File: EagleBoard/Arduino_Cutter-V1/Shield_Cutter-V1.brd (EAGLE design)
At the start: 68.9 x 53.7 mm, 82 parts, among them IC1 L298P, IC2 REG1117, K1 AQY21SOP, K2 AQY21SOP, U1 ARDUINOR3-DIMENSION, X1 2514-, X2 22-23-2041, X3 22-23-2021, X4 22-23-2021

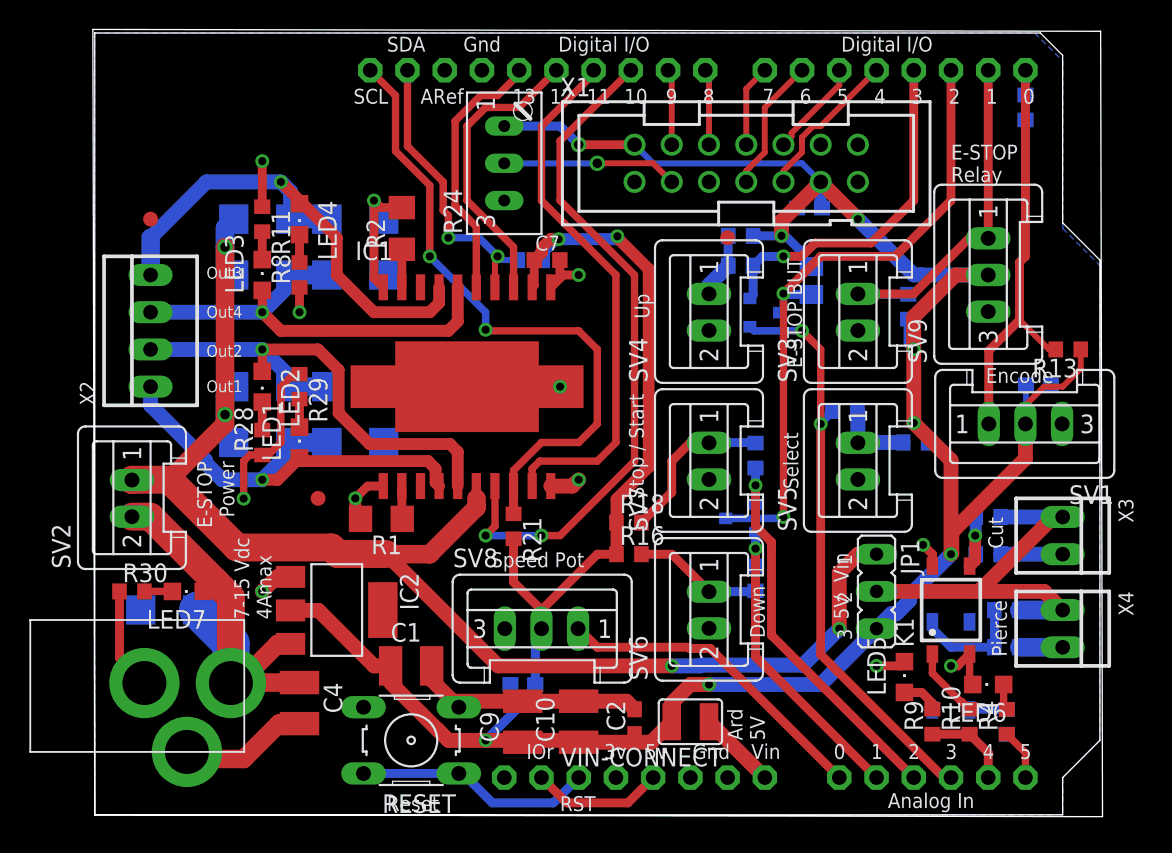
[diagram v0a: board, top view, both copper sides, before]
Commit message: FIX: increase components to 0805 size
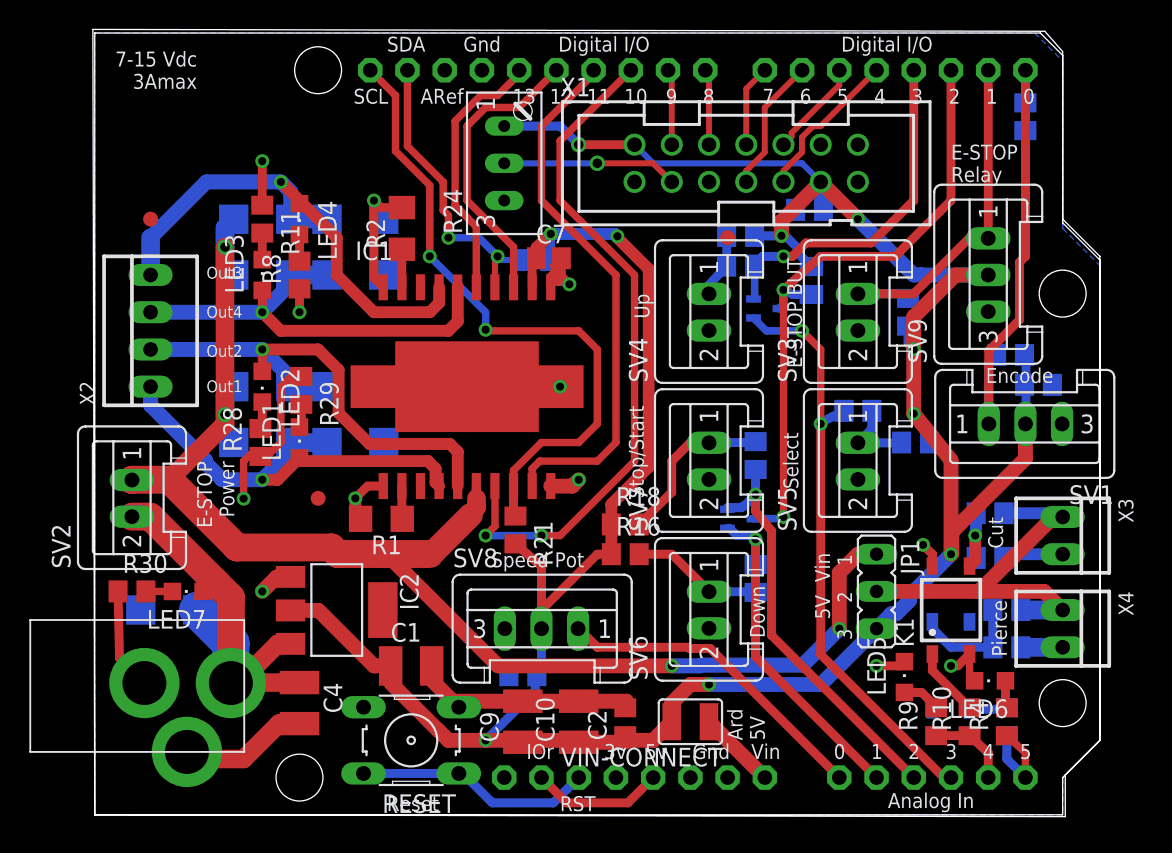
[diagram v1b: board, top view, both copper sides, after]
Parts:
- C11, C2, C5, C6: device rcl:C0603 -> rcl:C0805
- C7: device SmartPrj:C0603K -> SmartPrj:C0805
- D11, D12: device zetex:SOT-23 -> zetex:SOT323
- R10, R11, R12, R13, R14, R15, R16, R17, R18, R20, R21, R22, R23, R25, R26, R27, R28, R29, R3, R30, R4, R5, R6, R7, R8, R9: device resistor:R0603 -> resistor:R0805
- RESET: value (none) -> 1
- SV1, SV8, SV9: value (none) -> S3B-PH-K
- SV2, SV3, SV4, SV5, SV6, SV7: value (none) -> S2B-PH-K
- moved R13 3.96 mm to (62.5, 31.4), flipped to the bottom, turned to 0 degrees
- moved R25 0.89 mm to (52.1, 27.6)
- moved C11 0.63 mm to (29.2, 9.53)
- moved C2 0.63 mm to (36.2, 6.35)
- moved R14 0.63 mm to (63.5, 47.6)
- moved R20 0.38 mm to (55.5, 34.3)
- moved R22 0.38 mm to (30.1, 37.8)
- moved R12 0.28 mm to (61.1, 20.6)
- moved R3 0.28 mm to (61.1, 17.5)
- moved LED6 0.28 mm to (61.1, 9.14)
- moved R29 0.28 mm to (14.1, 29.0)
- moved D11 0.28 mm to (45.8, 34.5), turned to 90 degrees
- moved R21 0.28 mm to (28.7, 19.4)
- moved R18 0.28 mm to (36.2, 19.8)
- moved R9 0.25 mm to (57.4, 6.35)
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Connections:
- net SELECT_BUT: now also D11.2; no longer D11.3
- net UP_BUT: now also D11.3; no longer D11.2
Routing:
- net GND: track 95.8 -> 91.1 mm
- net SOL_PIERCE: track 3.49 -> 6.80 mm
- net DOWN_BUT: track 21.3 -> 23.6 mm
- net ENCODER1: track 30.2 -> 32.3 mm
- net BUTTON_INT: track 45.5 -> 43.7 mm
- net +5V: track 213.4 -> 212.1 mm
- net ENABLEA: track 44.2 -> 45.4 mm
- net RUN_BUT: track 26.9 -> 27.8 mm
- net SELECT_BUT: track 39.9 -> 40.5 mm
- net N$16: track 4.78 -> 5.29 mm
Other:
- board size 68.9 x 53.7 mm -> 68.7 x 53.7 mm
- board text added: "7-15 Vdc 3Amax"
- board text added: "CUT1-V1.0 8-17"
- board text added: "Stop/Start"
- board text removed: "7-15 Vdc 4Amax"
- board text removed: "CUT1-V1.0"
- board text removed: "Stop / Start"

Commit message: Chore: gerbers and files for pcb manufacture
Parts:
- removed LED7: Green, led:CHIPLED_0805
- removed R30: 1kΩ, resistor:R0805
- added X5: 22-23-2021, con-molex:22-23-2021
- moved FID3 6.98 mm to (3.81, 47.6)
- moved SV2 4.49 mm to (3.17, 26.0)
- moved X2 4.49 mm to (3.17, 37.5)
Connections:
- removed net N$18: LED7.C, R30.2
- removed net OUT5: C4.1, D10.P$1, IC2.3, LED7.A, SV2.2, U$2.TIP
- new net FUSE_RETURN: C4.1, D10.P$1, IC2.3, SV2.2, X5.2
- new net POWERIN: U$2.TIP, X5.1
- net GND: no longer R30.1
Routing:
- net OUT5: track 31.2 -> 0.00 mm
- net FUSE_RETURN: track 0.00 -> 30.3 mm
- net POWERIN: track 0.00 -> 10.8 mm
- net VMOT: track 96.5 -> 102.6 mm
- net GND: track 91.1 -> 86.2 mm
- net OUT1: track 31.1 -> 35.8 mm
- net OUT3: track 37.6 -> 34.9 mm
- net OUT4: track 31.7 -> 34.2 mm
- net OUT2: track 34.9 -> 37.3 mm
- net N$18: track 1.81 -> 0.00 mm
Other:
- board text added: "Encoder"
- board text added: "Fuse"
- board text added: "Sol 1"
- board text added: "Sol 2"
- board text removed: "Cut"
- board text removed: "Encode"
- board text removed: "Pierce"

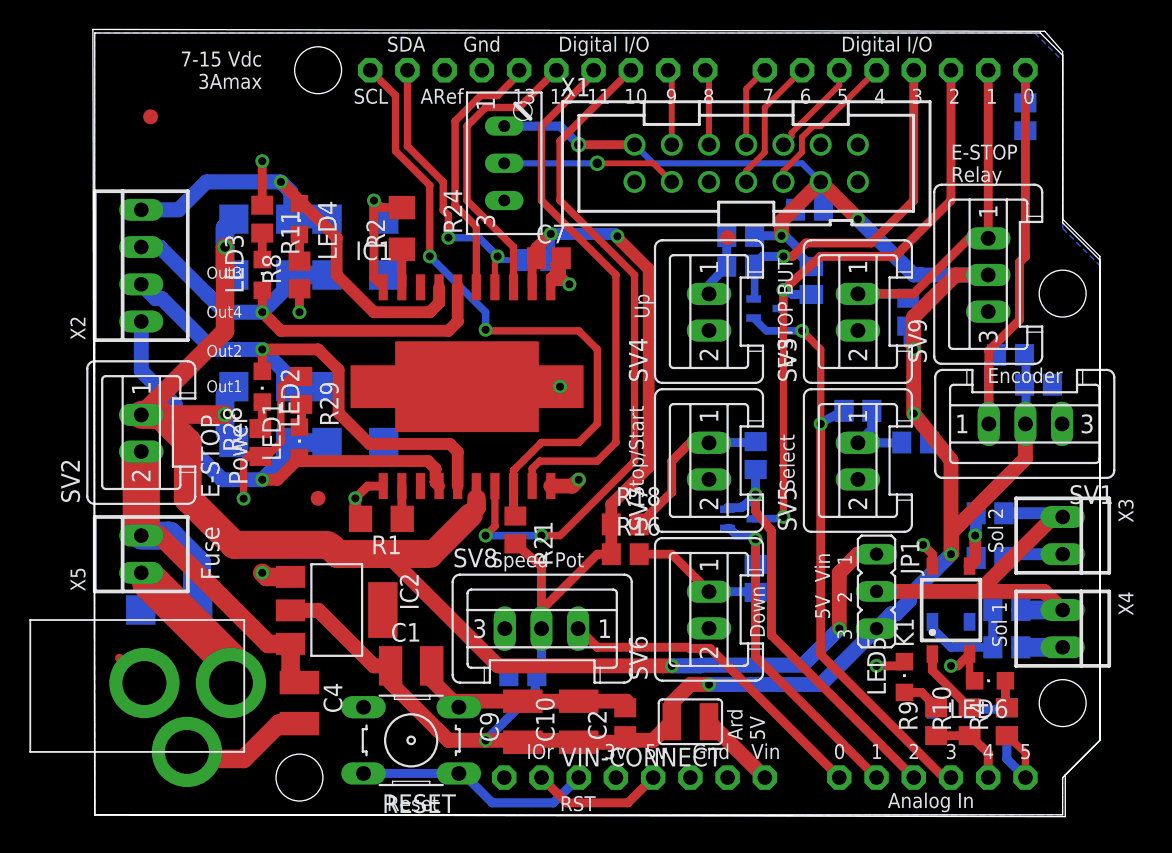
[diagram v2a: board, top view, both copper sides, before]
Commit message: Chore: add part names to pcb and cap from vmot to ground
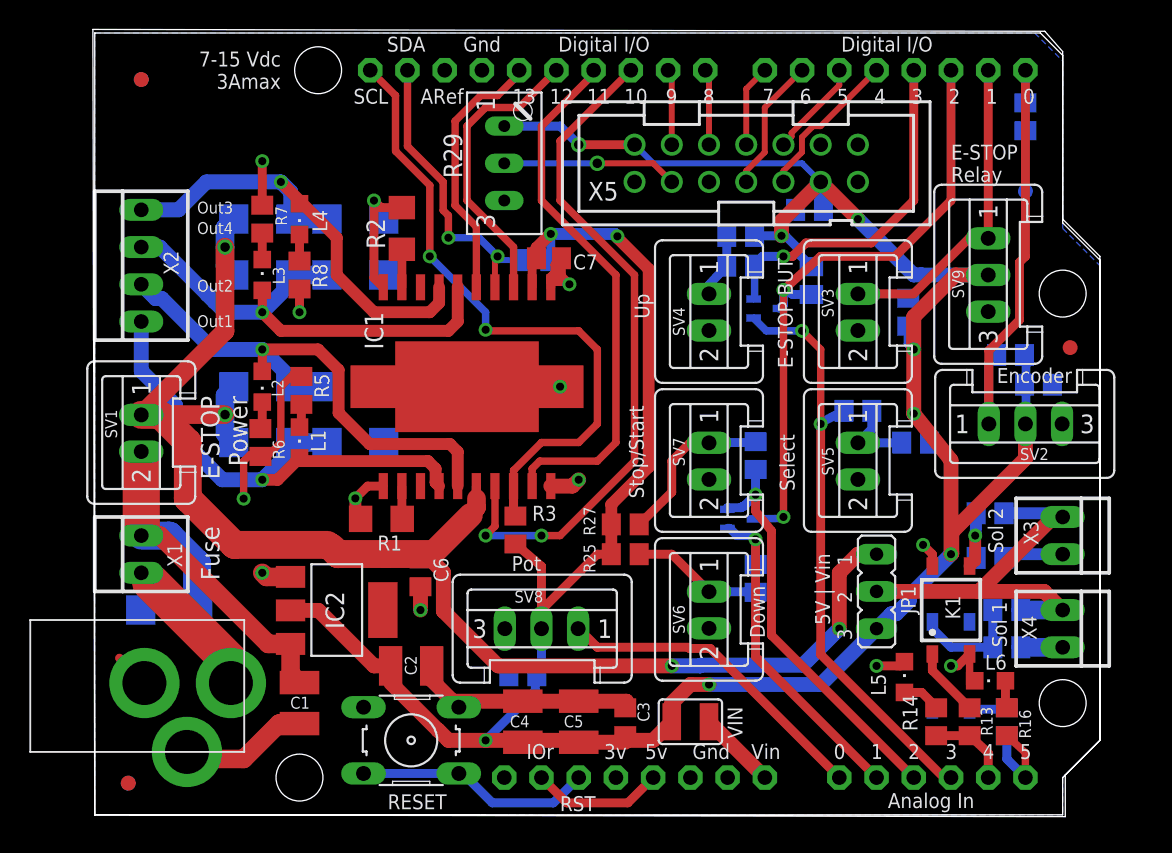
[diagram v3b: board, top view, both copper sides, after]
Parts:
- removed C11: 100nF, rcl:C0805
- removed D12: 40v, zetex:SOT323
- added C3, C8: 100nF, rcl:C0805
- added D9: SS14, SmartPrj:SMA
- added FID4, FID5, FID6: FIDUCIALMOUNT, SmartPrj:FIDUCIA-MOUNT
- C10, C9: value 10u 35V -> 100nF; device SmartPrj:C1210 -> rcl:C0805
- C2, C5: value 100nF -> 10u 35V; device rcl:C0805 -> SmartPrj:C1210
- C7: value 100n -> 100nF
- D10: value SS14 -> 40v; device SmartPrj:SMA -> zetex:SOT323
- R10: value 2.5kΩ -> 10kΩ
- R11, R28: value 1kΩ -> 10Ω
- R13, R14, R15, R16: value 10kΩ -> 330Ω
- R19: device resistor:M0805 -> resistor:R0805
- R21: value 10kΩ -> 10Ω
- R22: device resistor:R0805 -> resistor:M0805
- R23, R25, R27, R3: value 10Ω -> 10kΩ
- R24: value 10k -> 10Ω; device pot:S64W -> resistor:R0805
- R29: value 1kΩ -> 10k; device resistor:R0805 -> pot:S64W
- R4: value 300Ω -> 10kΩ
- R5: value 10kΩ -> 1kΩ
- R6: value 2.5kΩ -> 1kΩ
- R7: value 10Ω -> 1kΩ
- R9: value 300Ω -> 10Ω
- SV1: value S3B-PH-K -> S2B-PH-K; device con-amp-mt:S03P -> con-amp-mt:S02P
- SV2: value S2B-PH-K -> S3B-PH-K; device con-amp-mt:S02P -> con-amp-mt:S03P
- X1: value 2514- -> 22-23-2021; device con-3m:PAK100/2500-14 -> con-molex:22-23-2021
- X5: value 22-23-2021 -> 2514-; device con-molex:22-23-2021 -> con-3m:PAK100/2500-14
- moved SV1 60.3 mm to (3.17, 26.0), turned to 90 degrees
- moved SV2 60.3 mm to (63.5, 26.7), turned to 180 degrees
- moved R11 58.6 mm to (62.2, 11.4), flipped to the bottom, turned to 180 degrees
- moved R7 58.6 mm to (11.4, 40.6), flipped to the top, turned to 270 degrees
- moved R6 54.4 mm to (11.3, 25.4), flipped to the top
- moved R5 50.4 mm to (14.1, 29.0), flipped to the top, turned to 270 degrees
- moved X1 49.1 mm to (3.17, 17.8), turned to 90 degrees
- moved X5 49.1 mm to (44.5, 44.5), turned to 0 degrees
- moved D10 45.7 mm to (45.8, 34.5), turned to 90 degrees
- moved R4 45.0 mm to (30.1, 37.8), flipped to the bottom, turned to 0 degrees
- moved R14 41.7 mm to (57.4, 6.35), flipped to the top
- moved C5 38.9 mm to (33.0, 6.35), flipped to the top, turned to 90 degrees
- moved C10 38.3 mm to (48.8, 41.3), flipped to the bottom, turned to 180 degrees
- moved R15 37.8 mm to (62.2, 6.35), turned to 90 degrees
- moved C6 36.3 mm to (22.2, 16.5), flipped to the top, turned to 90 degrees
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- renumbered LED1 to L1, LED2 to L2, LED3 to L3, LED4 to L4, LED5 to L5, LED6 to L6, VIN-CONNECT to VIN
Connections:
- net +5V: now also C10.2, C3.1, C4.1, C8.1, R23.1, R25.1, R27.1, R29.A, R3.2, R4.1, SV2.2, X5.11, X5.2; no longer C1.1, C10.1, C11.1, C6.2, R13.1, R15.1, R16.1, R17.1, R21.2, R24.A, SV1.2, X1.11, X1.2
- net BUTTON_INT: now also D10.1, R22.2; no longer D12.1, R19.2
- net DOWN_BUT: now also D11.2; no longer D12.2
- net E-STOP: now also R19.2; no longer R20.2
- net ENABLEA: now also R3.1; no longer R21.1
- net ENABLEB: now also R4.2; no longer R22.2
- net ENCODER1: now also R17.2, R18.2, SV2.1; no longer R13.2, R14.2, SV1.1
- net FUSE_RETURN: now also C1.1, D9.P$1, SV1.2, X1.2; no longer C4.1, D10.P$1, SV2.2, X5.2
- net GND: now also C10.1, C3.2, C8.2, D9.P$2, R17.1, R29.E, R5.1, R6.1, R7.1, SV2.3, X5.1, X5.12, X5.5; no longer C10.2, C11.2, D10.P$2, R11.1, R14.1, R24.E, R28.1, R29.1, SV1.3, X1.1, X1.12, X1.5
- net LCD_D4: now also X5.8; no longer X1.8
- net LCD_D5: now also X5.7; no longer X1.7
- net LCD_D6: now also X5.10; no longer X1.10
- net LCD_D7: now also X5.9; no longer X1.9
- net LCD_EN: now also X5.6; no longer X1.6
- net LCD_RS: now also X5.4; no longer X1.4
- net N$10: now also R10.2; no longer R5.2
- net N$11: now also R11.1, R12.1; no longer R5.1, R7.1
- net N$12: now also R16.2; no longer R4.2
- net N$13: now also R20.2, R21.1; no longer R15.2, R23.1
- net N$14: now also R15.2; no longer R6.2
- net N$15: now also R11.2; no longer R7.2
- net N$16: now also R10.1, R9.1; no longer R12.1, R3.1
- net N$17: now also R25.2; no longer R16.2
- net N$19: now also R27.2, R28.1; no longer R18.2, R27.1
- net N$2: now also R7.2; no longer R11.2
- net N$3: now also R6.2; no longer R28.2
- net N$4: now also R5.2; no longer R29.2
- net N$5: now also R13.2; no longer R10.2
- net N$7: now also R14.2; no longer R9.2
- net N$8: now also R9.2; no longer R3.2
- net N$9: now also R23.2, R24.1; no longer R17.2, R25.1
- net POWERIN: now also X1.1; no longer X5.1
- net RUN_BUT: now also D11.3, R28.2; no longer D12.3, R27.2
- net SELECT_BUT: now also D10.2, R24.2; no longer D11.2, R25.2
- net SOL_CUT: now also R13.1, R14.1; no longer R10.1, R9.1
- net SOL_PIERCE: now also R15.1, R16.1; no longer R4.1, R6.1
- net UP_BUT: now also D10.3, R21.2; no longer D11.3, R23.2
- net V0: now also R29.S, X5.3; no longer R24.S, X1.3
- net VMOT: now also C6.2, SV1.1; no longer SV2.1
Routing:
- net GND: track 86.2 -> 87.8 mm, vias 11 -> 12
- net VMOT: track 102.6 -> 102.1 mm
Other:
- board text added: "5V | Vin"
- board text added: "Pot"
- board text removed: "5V"
- board text removed: "Ard 5V"
- board text removed: "Reset"
- board text removed: "Speed Pot"
- board text removed: "Vin"

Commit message: Fix: fix floating ground. Feat: add power input terminal.
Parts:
- removed SV1: S2B-PH-K, con-amp-mt:S02P
- added X6: 22-23-2021, con-molex:22-23-2021
- X1: value 22-23-2021 -> 22-23-2041; device con-molex:22-23-2021 -> con-molex:22-23-2041
- moved X1 1.90 mm to (3.17, 19.7)
- moved D9 0.63 mm to (5.08, 13.3)
- turned JP1 to 90 degrees
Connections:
- net FUSE_RETURN: now also X1.4, X6.1; no longer SV1.2, X1.2
- net GND: now also X1.1
- net POWERIN: now also X1.2, X1.3; no longer X1.1
- net VMOT: now also X6.2; no longer SV1.1
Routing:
- net VMOT: track 102.1 -> 94.5 mm, vias 4 -> 3
- net POWERIN: track 10.8 -> 15.9 mm
- net FUSE_RETURN: track 30.3 -> 26.5 mm, vias 0 -> 1
- net GND: track 87.8 -> 84.3 mm, vias 12 -> 28
- net +5V: track 212.1 -> 212.9 mm
- net OUT1: track 35.8 -> 36.4 mm
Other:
- board text added: "CUT1-V1.1 8-17"
- board text added: "GND"
- board text added: "V+"
- board text added: "Vin | 5V"
- board text removed: "5V | Vin"
- board text removed: "CUT1-V1.0 8-17"

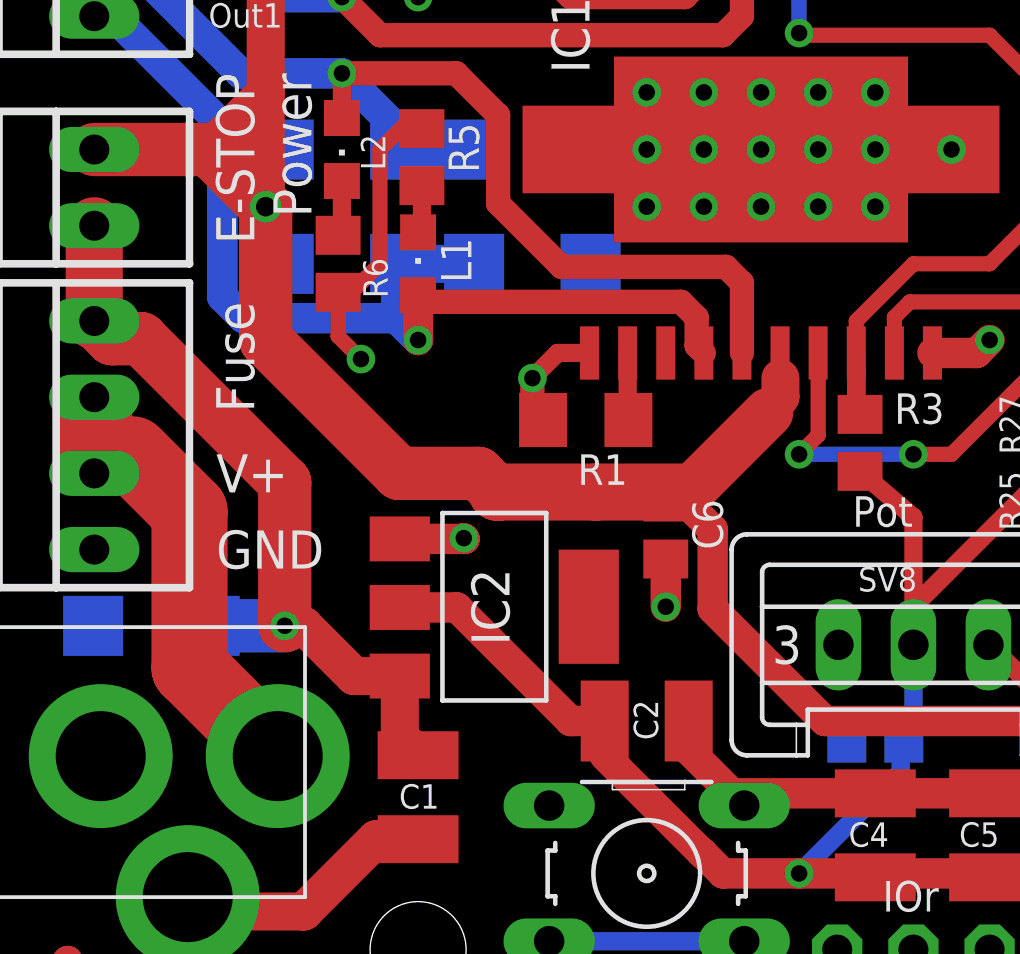
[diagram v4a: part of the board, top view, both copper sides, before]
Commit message: Feat: add fuse to 5v power
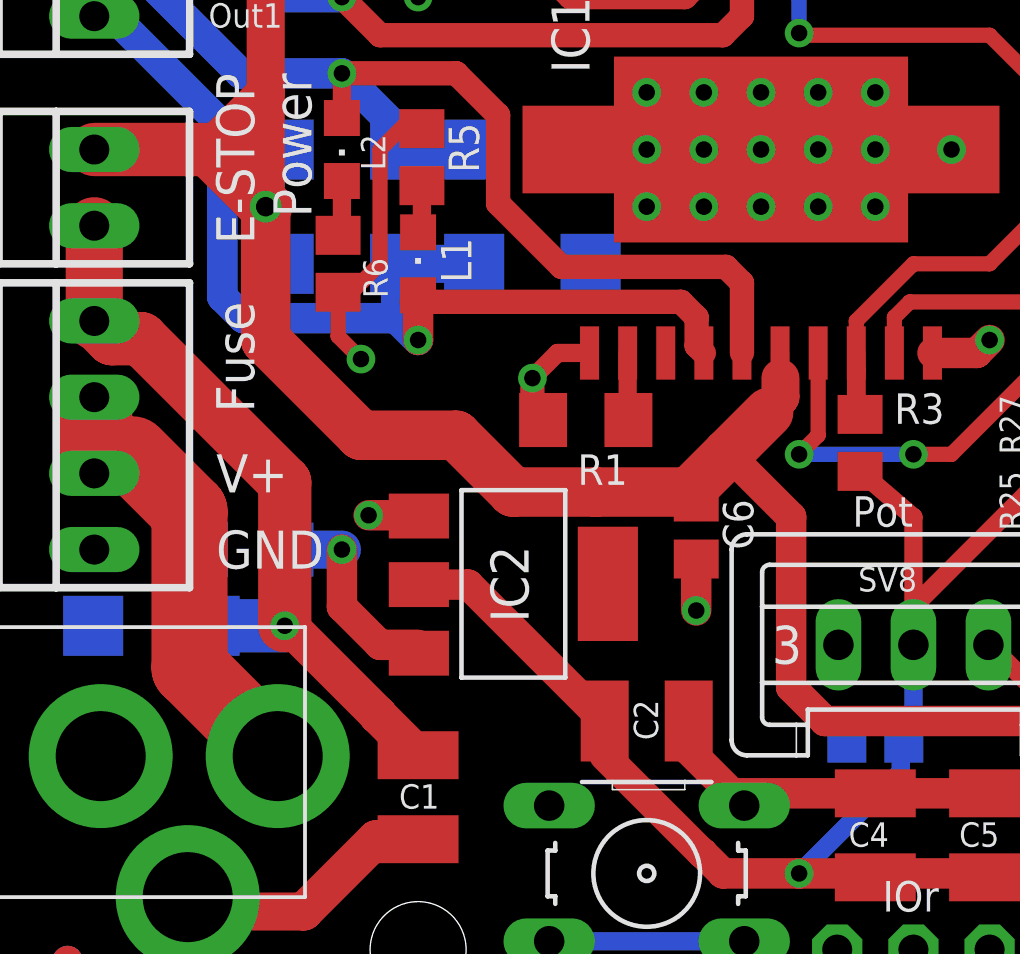
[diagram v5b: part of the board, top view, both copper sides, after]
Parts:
- added F1: 750mA, SmartPrj:R1206
- moved C6 1.02 mm to (23.2, 16.5)
- moved IC2 0.99 mm to (17.1, 14.7)
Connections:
- new net N$18: F1.1, IC2.3
- net FUSE_RETURN: now also F1.2; no longer IC2.3
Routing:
- net N$18: track 0.00 -> 7.03 mm, vias 0 -> 1
- net VMOT: track 94.5 -> 96.4 mm
- net FUSE_RETURN: track 26.5 -> 27.9 mm
